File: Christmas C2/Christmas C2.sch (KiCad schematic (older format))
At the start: 9 parts, among them J1 A_LEFT, J2 A_RIGHT, J3 B_LEFT, J4 B_RIGHT, J5 PWR_EXT, M1 Mounting, M2 Mounting, M3 Mounting, M4 Mounting

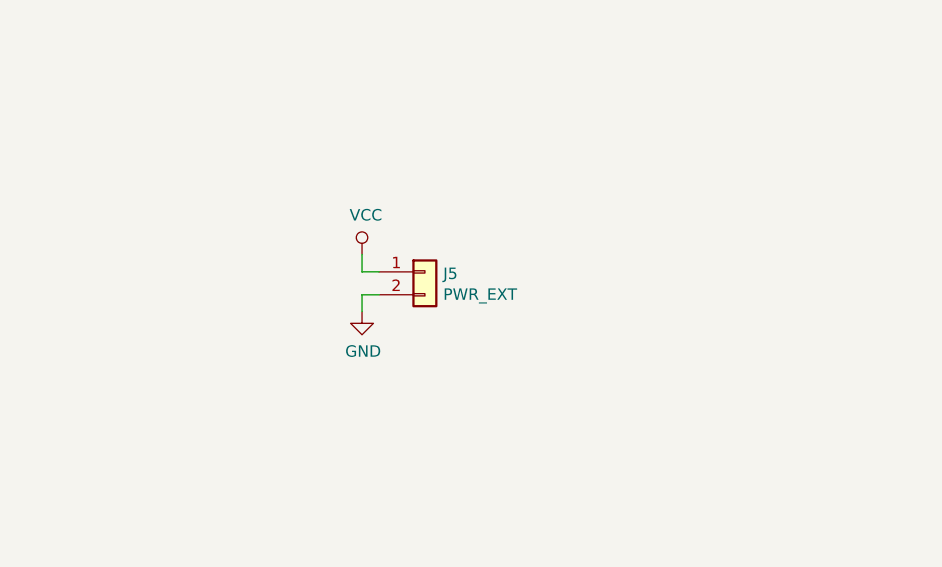
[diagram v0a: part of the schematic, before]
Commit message: Added MicroUSB breakout adapter and battery option to static board
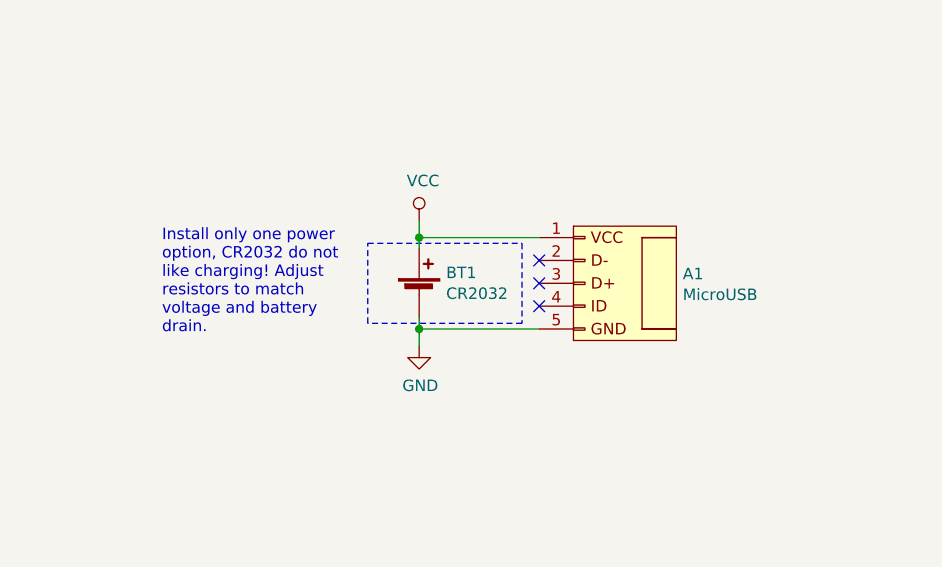
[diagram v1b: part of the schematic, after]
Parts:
- removed J5: PWR_EXT, Pin_Headers:Pin_Header_Straight_1x02_Pitch2.54mm, symbol Connector_Generic:Conn_01x02
- added A1: MicroUSB, christmas:microusb_breakout, symbol microusb_breakout:MicroUSB
- added BT1: CR2032, Battery_Holders:Keystone_103_1x20mm-CoinCell, symbol Device:Battery_Cell
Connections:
- net GND: now also A1.5 (GND), BT1.2 (-)
- net VCC: now also A1.1 (VCC), BT1.1 (+)
- no-connect marks 1 -> 4
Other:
- note added: "Install only one power\noption, CR2032 do not\nlike charging! Adjust\nresistors to match \nvoltage and battery\ndrain."
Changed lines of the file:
@@
 	1    0    0    -1
 $EndComp
-$Comp
-L Connector_Generic:Conn_01x02 J5
-U 1 1 5F8DBF59
-P 7425 2300
-F 0 "J5" H 7505 2292 50  0000 L CNN
-F 1 "PWR_EXT" H 7505 2201 50  0000 L CNN
-F 2 "Pin_Headers:Pin_Header_Straight_1x02_Pitch2.54mm" H 7425 2300 50  0001 C CNN
-F 3 "~" H 7425 2300 50  0001 C CNN
-	1    7425 2300
-	1    0    0    -1
-$EndComp
-Wire Wire Line
-	7150 2225 7150 2300
-Wire Wire Line
-	7150 2300 7225 2300
+Wire Wire Line
+	7400 2075 7400 2150
 $Comp
 L power:GND #PWR0108
 U 1 1 5F8DF23D
-P 7150 2475
-F 0 "#PWR0108" H 7150 2225 50  0001 C CNN
-F 1 "GND" H 7155 2302 50  0000 C CNN
-F 2 "" H 7150 2475 50  0001 C CNN
-F 3 "" H 7150 2475 50  0001 C CNN
-	1    7150 2475
-	1    0    0    -1
-$EndComp
-Wire Wire Line
-	7150 2475 7150 2400
-Wire Wire Line
-	7150 2400 7225 2400
+P 7400 2625
+F 0 "#PWR0108" H 7400 2375 50  0001 C CNN
+F 1 "GND" H 7405 2452 50  0000 C CNN
+F 2 "" H 7400 2625 50  0001 C CNN
+F 3 "" H 7400 2625 50  0001 C CNN
+	1    7400 2625
+	1    0    0    -1
+$EndComp
+Wire Wire Line
+	7400 2625 7400 2550
 $Comp
 L mounting:Mounting M4
@@
 L power:VCC #PWR0101
 U 1 1 5FB12A76
-P 7150 2225
-F 0 "#PWR0101" H 7150 2075 50  0001 C CNN
-F 1 "VCC" H 7167 2398 50  0000 C CNN
-F 2 "" H 7150 2225 50  0001 C CNN
-F 3 "" H 7150 2225 50  0001 C CNN
-	1    7150 2225
+P 7400 2075
+F 0 "#PWR0101" H 7400 1925 50  0001 C CNN
+F 1 "VCC" H 7417 2248 50  0000 C CNN
+F 2 "" H 7400 2075 50  0001 C CNN
+F 3 "" H 7400 2075 50  0001 C CNN
+	1    7400 2075
 	1    0    0    -1
 $EndComp
@@
 Wire Wire Line
 	2550 2500 2550 2600
+$Comp
+L microusb_breakout:MicroUSB A1
+U 1 1 5FB128F2
+P 8125 2350
+F 0 "A1" H 8553 2391 50  0000 L CNN
+F 1 "MicroUSB" H 8553 2300 50  0000 L CNN
+F 2 "christmas:microusb_breakout" H 8125 2350 50  0001 C CNN
+F 3 "~" H 8125 2350 50  0001 C CNN
+	1    8125 2350
+	1    0    0    -1
+$EndComp
+NoConn ~ 7925 2250
+NoConn ~ 7925 2350
+NoConn ~ 7925 2450
+$Comp
+L Device:Battery_Cell BT1
+U 1 1 5FB1AA56
+P 7400 2400
+F 0 "BT1" H 7518 2496 50  0000 L CNN
+F 1 "CR2032" H 7518 2405 50  0000 L CNN
+F 2 "Battery_Holders:Keystone_103_1x20mm-CoinCell" V 7400 2460 50  0001 C CNN
+F 3 "~" V 7400 2460 50  0001 C CNN
+	1    7400 2400
+	1    0    0    -1
+$EndComp
+Wire Wire Line
+	7400 2200 7400 2150
+Wire Wire Line
+	7400 2500 7400 2550
+Connection ~ 7400 2150
+Connection ~ 7400 2550
+Wire Wire Line
+	7400 2550 7925 2550
+Wire Wire Line
+	7400 2150 7925 2150
+Wire Notes Line
+	7175 2175 7850 2175
+Wire Notes Line
+	7850 2175 7850 2525
+Wire Notes Line
+	7850 2525 7175 2525
+Wire Notes Line
+	7175 2525 7175 2175
+Text Notes 6275 2575 0    50   ~ 0
+Install only one power\noption, CR2032 do not\nlike charging! Adjust\nresistors to match \nvoltage and battery\ndrain.
 $EndSCHEMATC
